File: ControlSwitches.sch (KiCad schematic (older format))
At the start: 17 parts, among them J6 Backup, SW1 HAZARD, SW2 CRUISE_SET, SW3 CRUISE, SW4 F/R_SW, SW5 HEADLIGHT_SW, SW6 BACKUP_SW, SW7 TURN_SIGNAL_SW, SW8 REGEN_SW

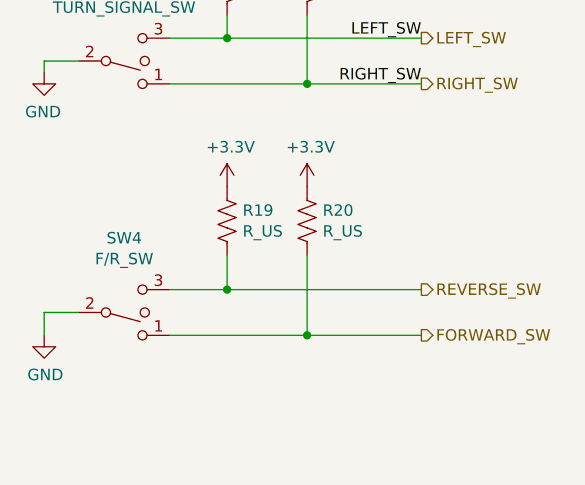
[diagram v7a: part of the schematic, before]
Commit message: Updated schematic with changed F/W switch and BPS_PWR direct connection to MinionConn
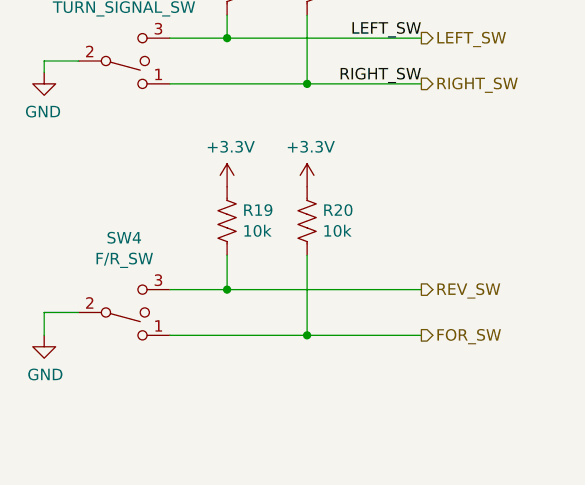
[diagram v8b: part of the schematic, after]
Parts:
- R19, R20: value R_US -> 10k; footprint (none) -> Resistor_SMD:R_0805_2012Metric
- SW4: footprint (none) -> Connector_Molex:Molex_Micro-Fit_3.0_43650-0300_1x03_P3.00mm_Horizontal
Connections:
- net FORWARD_SW renamed FOR_SW
- net REVERSE_SW renamed REV_SW
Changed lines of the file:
@@
 F 0 "SW4" H 7500 4475 50  0000 C CNN
 F 1 "F/R_SW" H 7500 4566 50  0000 C CNN
-F 2 "" H 7500 4800 50  0001 C CNN
+F 2 "Connector_Molex:Molex_Micro-Fit_3.0_43650-0300_1x03_P3.00mm_Horizontal" H 7500 4800 50  0001 C CNN
 F 3 "~" H 7500 4800 50  0001 C CNN
 	1    7500 4800
@@
 P 7950 4400
 F 0 "R19" H 8018 4446 50  0000 L CNN
-F 1 "R_US" H 8018 4355 50  0000 L CNN
-F 2 "" V 7990 4390 50  0001 C CNN
+F 1 "10k" H 8018 4355 50  0000 L CNN
+F 2 "Resistor_SMD:R_0805_2012Metric" V 7990 4390 50  0001 C CNN
 F 3 "~" H 7950 4400 50  0001 C CNN
 	1    7950 4400
@@
 P 8300 4400
 F 0 "R20" H 8368 4446 50  0000 L CNN
-F 1 "R_US" H 8368 4355 50  0000 L CNN
-F 2 "" V 8340 4390 50  0001 C CNN
+F 1 "10k" H 8368 4355 50  0000 L CNN
+F 2 "Resistor_SMD:R_0805_2012Metric" V 8340 4390 50  0001 C CNN
 F 3 "~" H 8300 4400 50  0001 C CNN
 	1    8300 4400
@@
 $EndComp
 Text HLabel 8800 4700 2    50   Output ~ 0
-REVERSE_SW
+REV_SW
 Text HLabel 8800 4900 2    50   Output ~ 0
-FORWARD_SW
+FOR_SW
 Wire Wire Line
 	7700 4700 7950 4700
